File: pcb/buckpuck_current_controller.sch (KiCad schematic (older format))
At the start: 18 parts, among them P1 POWER, P13 CONN_1, P14 CONN_1, P15 CONN_1, P16 CONN_1, P17 CONN_1, P2 ResetOverride, P3 SetSwitch, P4 Display, U1 V7809, U2 ARDUINO_NANO

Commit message: Finished version 1.1
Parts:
- added P13: SetSwitch, symbol CONN_2
- P3: value SetSwitch -> DisplaySwitch
- renumbered P13 to P14, P14 to P15, P15 to P16, P16 to P17, P17 to P18
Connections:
- net GND: now also P13.2 (PM)
- net at U2.16 (D13(PB5)(SCK)): now also P13.1 (P1)
- no-connect marks 8 -> 7
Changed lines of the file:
@@
-EESchema Schematic File Version 2  date Fri 20 May 2011 05:25:28 PM PDT
+EESchema Schematic File Version 2  date Tue 24 May 2011 02:48:27 PM PDT
 LIBS:power
 LIBS:device
@@
 Sheet 1 5
 Title "Buckpuck Current Controller"
-Date "21 may 2011"
+Date "24 may 2011"
 Rev "1.0"
 Comp ""
@@
 Comment4 ""
 $EndDescr
+Wire Wire Line
+	4500 5400 4500 5200
+Wire Wire Line
+	4500 5200 4650 5200
 Connection ~ 6050 5400
 Wire Wire Line
@@
 	3450 1900 3450 1500
 Wire Wire Line
-	1350 950  1350 1800
+	1350 1800 1350 950
 Wire Wire Line
 	1350 1800 1100 1800
@@
 	1350 2650 1350 1900
 Wire Wire Line
-	2500 950  1350 950
+	1350 950  2500 950
 Wire Wire Line
 	3450 2900 3450 2300
@@
 	2050 5700 2250 5700
 Wire Wire Line
-	6050 4950 6250 4950
-Wire Wire Line
-	6050 5900 6050 4950
+	6250 4950 6050 4950
+Wire Wire Line
+	6050 4950 6050 5900
 Wire Wire Line
 	6250 5250 6050 5250
@@
 	6250 5550 6050 5550
 Connection ~ 6050 5550
+Wire Wire Line
+	4650 5000 4350 5000
 $Comp
 L GND #PWR01
+U 1 1 4DDC25C5
+P 4500 5400
+F 0 "#PWR01" H 4500 5400 30  0001 C CNN
+F 1 "GND" H 4500 5330 30  0001 C CNN
+	1    4500 5400
+	1    0    0    -1
+$EndComp
+$Comp
+L CONN_2 P13
+U 1 1 4DDC2584
+P 5000 5100
+F 0 "P13" V 4950 5100 40  0000 C CNN
+F 1 "SetSwitch" V 5050 5100 40  0000 C CNN
+	1    5000 5100
+	1    0    0    -1
+$EndComp
+$Comp
+L GND #PWR02
 U 1 1 4DD6F401
 P 6050 5900
-F 0 "#PWR01" H 6050 5900 30  0001 C CNN
+F 0 "#PWR02" H 6050 5900 30  0001 C CNN
 F 1 "GND" H 6050 5830 30  0001 C CNN
 	1    6050 5900
@@
 $EndComp
 $Comp
-L CONN_1 P17
+L CONN_1 P18
 U 1 1 4DD6F3EE
 P 6400 5550
-F 0 "P17" H 6480 5550 40  0000 L CNN
+F 0 "P18" H 6480 5550 40  0000 L CNN
 F 1 "CONN_1" H 6400 5605 30  0001 C CNN
 	1    6400 5550
@@
 $EndComp
 $Comp
-L CONN_1 P16
+L CONN_1 P17
 U 1 1 4DD6F3EB
 P 6400 5400
-F 0 "P16" H 6480 5400 40  0000 L CNN
+F 0 "P17" H 6480 5400 40  0000 L CNN
 F 1 "CONN_1" H 6400 5455 30  0001 C CNN
 	1    6400 5400
@@
 $EndComp
 $Comp
-L CONN_1 P15
+L CONN_1 P16
 U 1 1 4DD6F3E8
 P 6400 5250
-F 0 "P15" H 6480 5250 40  0000 L CNN
+F 0 "P16" H 6480 5250 40  0000 L CNN
 F 1 "CONN_1" H 6400 5305 30  0001 C CNN
 	1    6400 5250
@@
 $EndComp
 $Comp
-L CONN_1 P14
+L CONN_1 P15
 U 1 1 4DD6F3E5
 P 6400 5100
-F 0 "P14" H 6480 5100 40  0000 L CNN
+F 0 "P15" H 6480 5100 40  0000 L CNN
 F 1 "CONN_1" H 6400 5155 30  0001 C CNN
 	1    6400 5100
@@
 $EndComp
 $Comp
-L CONN_1 P13
+L CONN_1 P14
 U 1 1 4DD6F3DD
 P 6400 4950
-F 0 "P13" H 6480 4950 40  0000 L CNN
+F 0 "P14" H 6480 4950 40  0000 L CNN
 F 1 "CONN_1" H 6400 5005 30  0001 C CNN
 	1    6400 4950
@@
 P 2600 5800
 F 0 "P3" V 2550 5800 40  0000 C CNN
-F 1 "SetSwitch" V 2650 5800 40  0000 C CNN
+F 1 "DisplaySwitch" V 2650 5800 40  0000 C CNN
 	1    2600 5800
 	1    0    0    -1
 $EndComp
 $Comp
-L VDD #PWR02
+L VDD #PWR03
 U 1 1 4DD30F8E
 P 6550 1650
-F 0 "#PWR02" H 6550 1750 30  0001 C CNN
+F 0 "#PWR03" H 6550 1750 30  0001 C CNN
 F 1 "VDD" H 6550 1760 30  0000 C CNN
 	1    6550 1650
@@
 $EndComp
 $Comp
-L GND #PWR03
+L GND #PWR04
 U 1 1 4DD30F78
 P 5750 2450
-F 0 "#PWR03" H 5750 2450 30  0001 C CNN
+F 0 "#PWR04" H 5750 2450 30  0001 C CNN
 F 1 "GND" H 5750 2380 30  0001 C CNN
 	1    5750 2450
@@
 $EndComp
 $Comp
-L GND #PWR04
+L GND #PWR05
 U 1 1 4DD30F74
 P 4250 2450
-F 0 "#PWR04" H 4250 2450 30  0001 C CNN
+F 0 "#PWR05" H 4250 2450 30  0001 C CNN
 F 1 "GND" H 4250 2380 30  0001 C CNN
 	1    4250 2450
@@
 $EndComp
 $Comp
-L GND #PWR05
+L GND #PWR06
 U 1 1 4DD30F46
 P 5000 2250
-F 0 "#PWR05" H 5000 2250 30  0001 C CNN
+F 0 "#PWR06" H 5000 2250 30  0001 C CNN
 F 1 "GND" H 5000 2180 30  0001 C CNN
 	1    5000 2250
@@
 $EndComp
 $Comp
-L +5V #PWR06
+L +5V #PWR07
 U 1 1 4DD308A2
 P 5750 3250
-F 0 "#PWR06" H 5750 3340 20  0001 C CNN
+F 0 "#PWR07" H 5750 3340 20  0001 C CNN
 F 1 "+5V" H 5750 3340 30  0000 C CNN
 	1    5750 3250
@@
 $EndComp
 $Comp
-L PWR_FLAG #FLG07
+L PWR_FLAG #FLG08
 U 1 1 4DD3088D
 P 5700 3850
-F 0 "#FLG07" H 5700 4120 30  0001 C CNN
+F 0 "#FLG08" H 5700 4120 30  0001 C CNN
 F 1 "PWR_FLAG" H 5700 4080 30  0000 C CNN
 	1    5700 3850
@@
 $EndComp
 $Comp
-L +5V #PWR08
+L +5V #PWR09
 U 1 1 4DD3087D
 P 5450 3700
-F 0 "#PWR08" H 5450 3790 20  0001 C CNN
+F 0 "#PWR09" H 5450 3790 20  0001 C CNN
 F 1 "+5V" H 5450 3790 30  0000 C CNN
 	1    5450 3700
@@
 $EndComp
 $Comp
-L VDD #PWR09
+L VDD #PWR010
 U 1 1 4DD3074D
 P 4450 2950
-F 0 "#PWR09" H 4450 3050 30  0001 C CNN
+F 0 "#PWR010" H 4450 3050 30  0001 C CNN
 F 1 "VDD" H 4450 3060 30  0000 C CNN
 	1    4450 2950
@@
 $EndComp
 $Comp
-L GND #PWR010
+L GND #PWR011
 U 1 1 4DD2FA71
 P 2250 6400
-F 0 "#PWR010" H 2250 6400 30  0001 C CNN
+F 0 "#PWR011" H 2250 6400 30  0001 C CNN
 F 1 "GND" H 2250 6330 30  0001 C CNN
 	1    2250 6400
@@
 DisplayRX
 $Comp
-L GND #PWR011
+L GND #PWR012
 U 1 1 4DD2F8D7
 P 3550 6350
-F 0 "#PWR011" H 3550 6350 30  0001 C CNN
+F 0 "#PWR012" H 3550 6350 30  0001 C CNN
 F 1 "GND" H 3550 6280 30  0001 C CNN
 	1    3550 6350
@@
 $EndComp
 $Comp
-L VDD #PWR012
+L VDD #PWR013
 U 1 1 4DD2F8C8
 P 4100 5750
-F 0 "#PWR012" H 4100 5850 30  0001 C CNN
+F 0 "#PWR013" H 4100 5850 30  0001 C CNN
 F 1 "VDD" H 4100 5860 30  0000 C CNN
 	1    4100 5750
@@
 $EndComp
 $Comp
-L GND #PWR013
+L GND #PWR014
 U 1 1 4DD2F728
 P 4600 3800
-F 0 "#PWR013" H 4600 3800 30  0001 C CNN
+F 0 "#PWR014" H 4600 3800 30  0001 C CNN
 F 1 "GND" H 4600 3730 30  0001 C CNN
 	1    4600 3800
@@
 $EndComp
 $Comp
-L GND #PWR014
+L GND #PWR015
 U 1 1 4DD2F63F
 P 6800 3600
-F 0 "#PWR014" H 6800 3600 30  0001 C CNN
+F 0 "#PWR015" H 6800 3600 30  0001 C CNN
 F 1 "GND" H 6800 3530 30  0001 C CNN
 	1    6800 3600
@@
 NoConn ~ 4350 4800
 NoConn ~ 4350 4900
-NoConn ~ 4350 5000
 Text Label 2000 4800 0    60   ~ 0
 OnOffSwitchC
@@
 DisplayRX
 $Comp
-L GND #PWR015
+L GND #PWR016
 U 1 1 4DB0D0E3
 P 1550 4000
-F 0 "#PWR015" H 1550 4000 30  0001 C CNN
+F 0 "#PWR016" H 1550 4000 30  0001 C CNN
 F 1 "GND" H 1550 3930 30  0001 C CNN
 	1    1550 4000
@@
 $EndComp
 $Comp
-L GND #PWR016
+L GND #PWR017
 U 1 1 4B884901
 P 3200 3050
-F 0 "#PWR016" H 3200 3050 30  0001 C CNN
+F 0 "#PWR017" H 3200 3050 30  0001 C CNN
 F 1 "GND" H 3200 2980 30  0001 C CNN
 	1    3200 3050
@@
 $EndComp
 $Comp
-L PWR_FLAG #FLG017
+L PWR_FLAG #FLG018
 U 1 1 4B61DEC3
 P 2950 2750
-F 0 "#FLG017" H 2950 3020 30  0001 C CNN
+F 0 "#FLG018" H 2950 3020 30  0001 C CNN
 F 1 "PWR_FLAG" H 2950 2980 30  0000 C CNN
 	1    2950 2750
@@
 $EndComp
 $Comp
-L PWR_FLAG #FLG018
+L PWR_FLAG #FLG019
 U 1 1 4B61DEA9
 P 2400 750
-F 0 "#FLG018" H 2400 1020 30  0001 C CNN
+F 0 "#FLG019" H 2400 1020 30  0001 C CNN
 F 1 "PWR_FLAG" H 2400 980 30  0000 C CNN
 	1    2400 750
@@
 $EndComp
 $Comp
-L PWR_FLAG #FLG019
+L PWR_FLAG #FLG020
 U 1 1 4B61DE8F
 P 3450 1500
-F 0 "#FLG019" H 3450 1770 30  0001 C CNN
+F 0 "#FLG020" H 3450 1770 30  0001 C CNN
 F 1 "PWR_FLAG" H 3450 1730 30  0000 C CNN
 	1    3450 1500

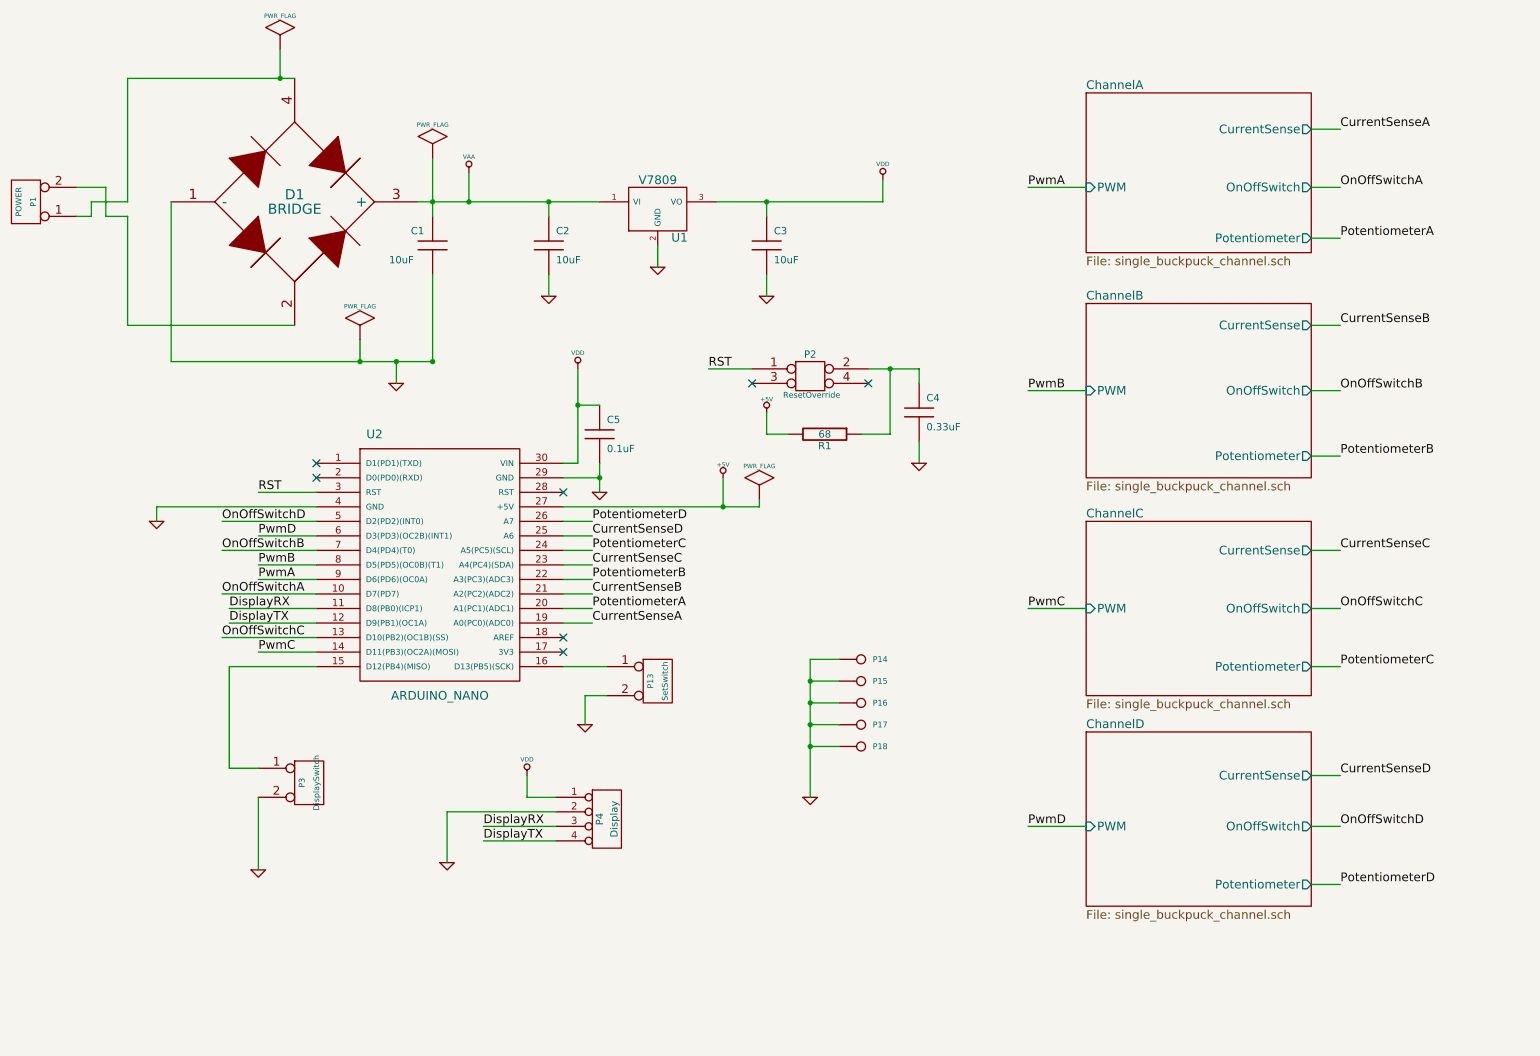
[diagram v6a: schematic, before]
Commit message: Modified schematic, board, and enclosure files
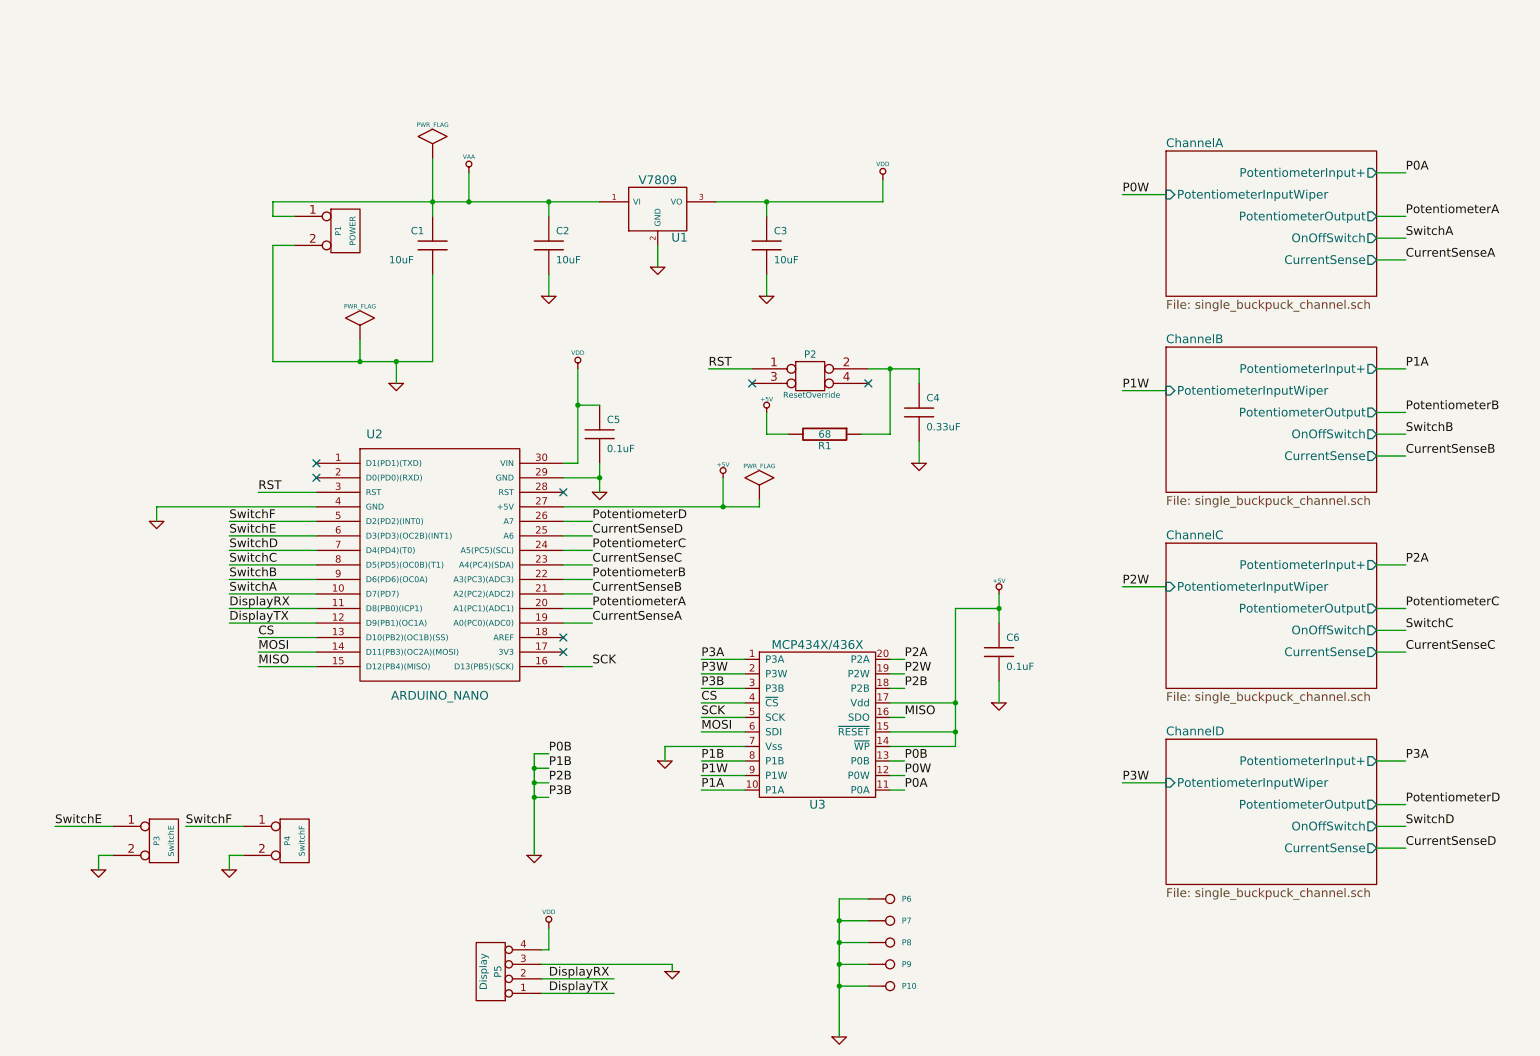
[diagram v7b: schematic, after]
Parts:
- removed D1: BRIDGE, symbol BRIDGE
- added C6: 0.1uF, symbol C
- added U3: MCP434X/436X, symbol MCP434X/436X
- P3: value DisplaySwitch -> SwitchE
- P4: renamed from P13; value SetSwitch -> SwitchF
- renumbered P18 to P10, P4 to P5, P14 to P6, P15 to P7, P16 to P8, P17 to P9
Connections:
- net +5V: now also C6.1, U3.14 (~WP), U3.15 (~RESET), U3.17 (Vdd)
- net DisplayRX: now also P5.2 (P2); no longer P5.3 (P3)
- net DisplayTX: now also P5.1 (P1); no longer P5.4 (P4)
- net GND: now also P1.2 (PM), P5.3 (P3), C6.2, U3.13 (P0B), U3.18 (P2B), U3.3 (P3B), U3.7 (Vss), U3.8 (P1B); no longer P5.2 (P2)
- net VAA: now also P1.1 (P1)
- net VDD: now also P5.4 (P4); no longer P5.1 (P1)
- net MISO: now reaches U2.15 (D12(PB4)(MISO))
- net MISO: now also U3.16 (SDO); no longer P3.1 (P1)
- net SCK: now reaches U2.16 (D13(PB5)(SCK))
- net SCK: now also U3.5 (SCK); no longer P4.1 (P1)
- net OnOffSwitchA renamed SwitchA
- net OnOffSwitchB renamed SwitchD
- net OnOffSwitchC renamed CS
- net CS: now also U3.4 (~CS)
- net OnOffSwitchD renamed SwitchF
- net SwitchF: now also P4.1 (P1)
- net PwmA renamed SwitchB
- net PwmB renamed SwitchC
- net PwmC renamed MOSI
- net MOSI: now also U3.6 (SDI)
- net PwmD renamed SwitchE
- net SwitchE: now also P3.1 (P1)
- new net P0A: U3.11 (P0A)
- new net P0W: U3.12 (P0W)
- new net P1A: U3.10 (P1A)
- new net P1W: U3.9 (P1W)
- new net P2A: U3.20 (P2A)
- new net P2W: U3.19 (P2W)
- new net P3A: U3.1 (P3A)
- new net P3W: U3.2 (P3W)
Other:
- moved on the sheet: P1, P10, P3, P4, P5, P6, P7, P8, P9

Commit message: Almost finished with version 2 board.
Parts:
- removed C5: 0.1uF, symbol C
- removed P10: CONN_1, symbol CONN_1
- removed P3: SwitchE, symbol CONN_2
- removed P4: SwitchF, symbol CONN_2
- added P4: Switches, symbol CONN_6X2
- renumbered C6 to C5, P5 to P3, P6 to P5, P7 to P6, P8 to P7, P9 to P8
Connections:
- net GND: now also P4.10, P4.12, P4.2 (P2), P4.4 (P4), P4.6 (P6), P4.8 (P8)
- net SwitchA: now also P4.1 (P1)
- net SwitchB: now also P4.3 (P3)
- net SwitchC: now also P4.5 (P5)
- net SwitchD: now also P4.7 (P7)
- net SwitchE: now also P4.9
- net SwitchF: now also P4.11
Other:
- moved on the sheet: P3, P5, P6, P7, P8
